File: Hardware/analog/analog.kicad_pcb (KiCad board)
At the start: 4 copper layers, 128 x 182 mm, 127 parts, among them J201 Würth 74651194R, J202 Würth 74651194R, J301 Conn_02x10_Odd_Even, J501 Conn_01x01, J502 Conn_01x01, M501 Fan_4pin, Q201 IXTH80N075L2, Q202 IXTH80N075L2, Q501 MMBT3904, U201 ADA4522-2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

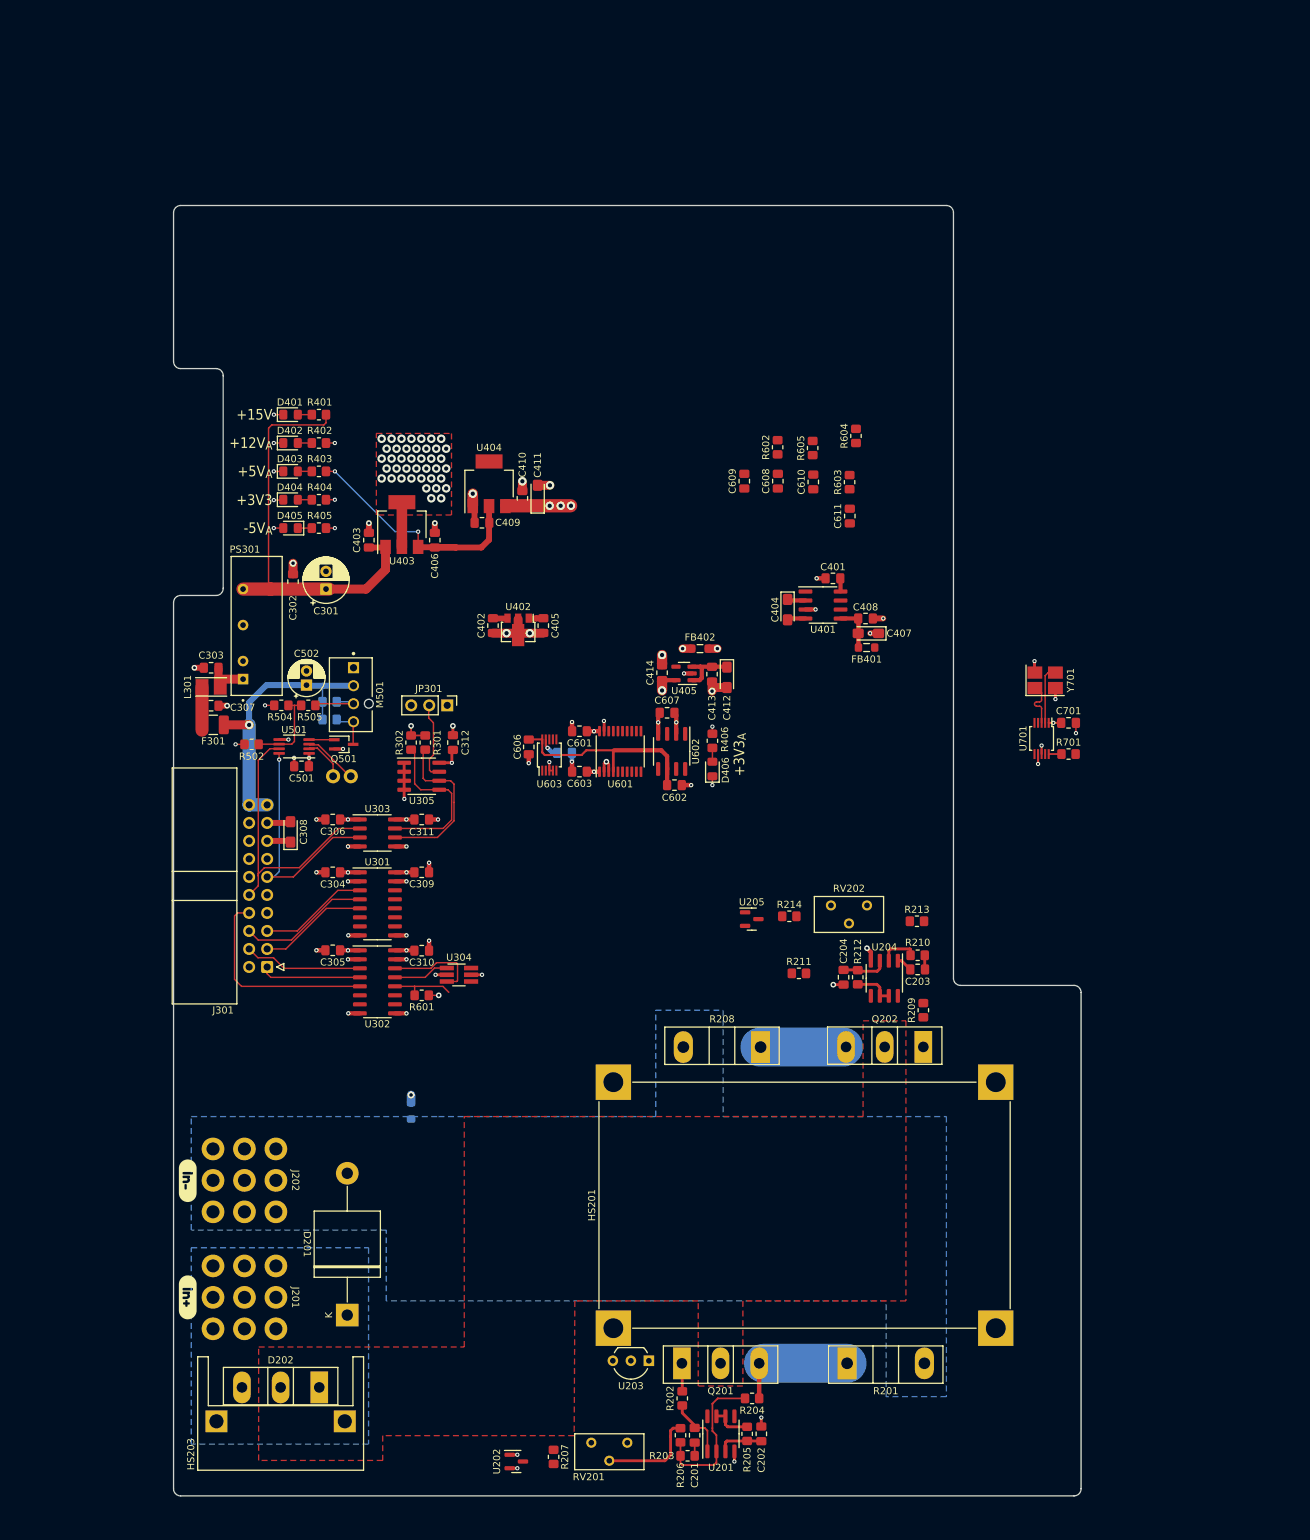
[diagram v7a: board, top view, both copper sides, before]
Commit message: Initial pass at analog board
- Everything currently in the schematic is routed, and stuff is
  reasonably sanely laid out

- Some compromises: namely, the zero offset doesn't use the DAC
  reference for its positive, but generates a separate 2.5V via the
  shunt diodes; this is then shared between both op-amps. That avoids
  the DAC/ADC reference getting noisified

  Also, we don't have an ADC for measuring the temperature sensors yet,
  and in fact, those aren't routed out (or existent really) yet either

- TODO: add test points for drive voltages and current sense voltages
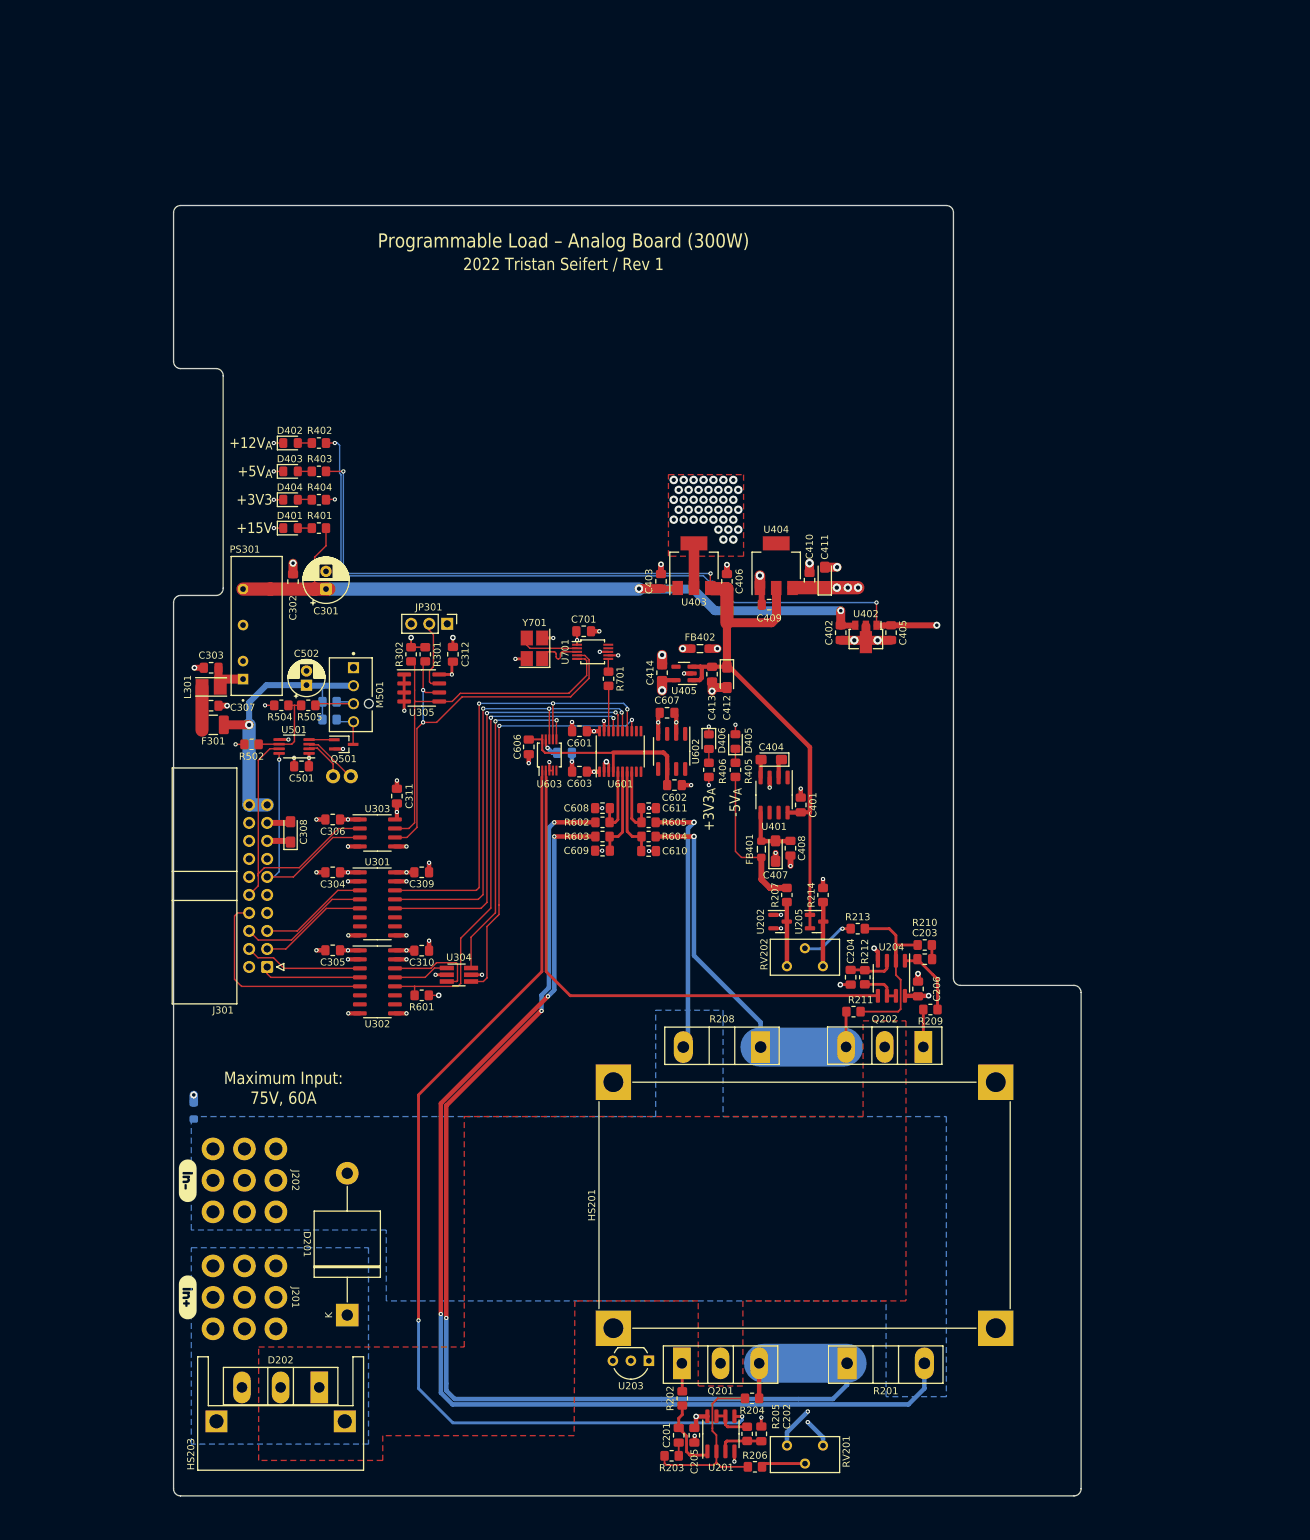
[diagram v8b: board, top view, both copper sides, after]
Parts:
- added C205: 100nF, Capacitor_SMD:C_0805_2012Metric_Pad1.18x1.45mm_HandSolder, F.Cu at (93.5, 193.4)
- added C206: 100nF, Capacitor_SMD:C_0805_2012Metric_Pad1.18x1.45mm_HandSolder, F.Cu at (125.0, 130.5)
- moved R207 85.8 mm to (106.5, 117.2)
- moved U202 84.8 mm to (105.5, 121.0)
- moved Y701 72.2 mm to (70.9, 82.5), turned to 90 degrees
- moved D405 69.6 mm to (99.2, 95.6), turned to 90 degrees
- moved C701 69.6 mm to (77.8, 80.0)
- moved R405 67.9 mm to (99.2, 99.6), turned to 90 degrees
- moved R701 65.7 mm to (81.3, 86.8), turned to -90 degrees
- moved U701 64.5 mm to (79.1, 83.0), turned to 0 degrees
- moved R604 63.6 mm to (87.0, 109.0), turned to 180 degrees
- moved R603 60.9 mm to (80.5, 109.0), turned to 0 degrees
- moved R602 58.4 mm to (80.5, 107.0), turned to 0 degrees
- moved R605 57.6 mm to (87.0, 107.0), turned to 180 degrees
- moved C610 57.0 mm to (87.0, 111.0), turned to 0 degrees
- moved C609 55.8 mm to (80.5, 111.0), turned to 0 degrees
- moved C608 52.3 mm to (80.5, 105.0), turned to 180 degrees
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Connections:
- Q201 pad 3: /MOSFET Load/ISense0 -> /ISense_{0
- Q202 pad 3: /MOSFET Load/ISense1 -> /ISense_{1
- R201 pad 1: /MOSFET Load/ISense0 -> /ISense_{0
- R204 pad 2: /MOSFET Load/ISense0 -> /ISense_{0
- R207 pad 1: Net-(R207-Pad1) -> /MOSFET Load/OffRef-
- R208 pad 1: /MOSFET Load/ISense1 -> /ISense_{1
- R211 pad 2: /MOSFET Load/ISense1 -> /ISense_{1
- R214 pad 1: Net-(R214-Pad1) -> /MOSFET Load/OffRef+
- R214 pad 2: -5VA -> GND
- R602 pad 1: /Analog stuff/ISense_{0+ -> /ISense_{0
- R603 pad 1: /Analog stuff/ISense_{0- -> GNDPWR
- R604 pad 1: /Analog stuff/ISense_{1+ -> /ISense_{1
- R605 pad 1: /Analog stuff/ISense_{1- -> GNDPWR
- RV201 pad 1: Net-(R207-Pad1) -> /MOSFET Load/OffRef-
- RV201 pad 3: /MOSFET Load/VREF -> /MOSFET Load/OffRef+
- RV202 pad 1: Net-(R214-Pad1) -> /MOSFET Load/OffRef-
- RV202 pad 3: /MOSFET Load/VREF -> /MOSFET Load/OffRef+
- U202 pad 3: Net-(R207-Pad1) -> /MOSFET Load/OffRef-
- U204 pad 5: /MOSFET Load/ISet_{1} -> /ISet_{1
- U205 pad 1: GND -> +5VA
- U205 pad 2: GND -> +5VA
- U205 pad 3: Net-(R214-Pad1) -> /MOSFET Load/OffRef+
- U701 pad 10: Net-(R701-Pad1) -> unconnected-(U701-Pad10)
- U701 pad 6: unconnected-(U701-Pad6) -> Net-(R701-Pad1)
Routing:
- net +12VA: track 3.34 -> 269.2 mm, vias 1 -> 5
- net GNDPWR: track 0.00 -> 202.0 mm, vias 0 -> 4
- net /ISense_{0: track 0.00 -> 169.8 mm, vias 0 -> 3
- net /ISet_{0: track 0.00 -> 143.8 mm, vias 0 -> 2
- net +5VA: track 46.8 -> 148.1 mm
- net /MOSFET Load/OffRef+: track 0.00 -> 78.7 mm, vias 0 -> 1
- net /MOSFET Load/OffRef-: track 0.00 -> 78.7 mm, vias 0 -> 1
- net /ISet_{1: track 0.00 -> 76.6 mm
- net /Analog stuff/SPI_SCK: track 0.00 -> 67.6 mm, vias 0 -> 3
- net /Analog stuff/SPI_MOSI: track 0.00 -> 65.9 mm, vias 0 -> 3
- net /Analog stuff/SPI_MISO: track 0.00 -> 61.0 mm, vias 0 -> 2
- net /Analog stuff/~{IRQ}: track 9.22 -> 69.3 mm, vias 0 -> 2
- net /Analog stuff/~{CS_ADC}: track 0.00 -> 59.4 mm, vias 0 -> 2
- net /ISense_{1: track 0.00 -> 55.8 mm, vias 0 -> 1
- net /Analog stuff/~{CS_DAC}: track 0.00 -> 47.6 mm, vias 0 -> 2
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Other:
- board text added: "2022 Tristan Seifert / Rev 1"
- board text added: "Maximum Input: 75V, 60A"
- board text added: "Programmable Load – Analog Board (300W)"
